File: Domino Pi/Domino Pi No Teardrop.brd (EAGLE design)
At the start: 71.1 x 33 mm, 73 parts, among them J1 MH28-1, J2 MH28-1, M1 DOMINO, SW1 IT-1100, U1 MP2162GQH, U2 CP2104-F03-GM, U3 74LVC1G125DCK

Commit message: Changed copyright
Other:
- board text added: "Reference designs are provided "AS IS" and "WITH ALL FAULTS". The Domino Team disclaims all other warranties express or implied, regarding this product, including but not limited to, any implied warranties of merchantibility or fitness for any particular application."
- board text added: "The Domino Team may make changes to specifications and product descriptions at any time, without notice."
- board text added: "© 2014, The Domino Team. All rights reserved."
- board text removed: "Michel Stempin may make changes to specifications and product descriptions at any time, without notice."
- board text removed: "Reference designs are provided "AS IS" and "WITH ALL FAULTS". Michel Stempin disclaims all other warranties express or implied, regarding this product, including but not limited to, any implied warranties of merchantibility or fitness for any particular application."
- board text removed: "© 2014, Michel Stempin. All rights reserved."
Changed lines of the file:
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@@
 See creativecommons.org/licenses/by-sa/4.0/</text>
 <text x="49.53" y="-50.8" size="0.8128" layer="48" ratio="20">Reference designs are provided "AS IS" and "WITH ALL FAULTS".
-Michel Stempin disclaims all other warranties express or implied,
+The Domino Team disclaims all other warranties express or implied,
 regarding this product, including but not limited to, any implied warranties of
 merchantibility or fitness for any particular application.</text>
-<text x="49.53" y="-54.61" size="0.8128" layer="48" ratio="20">Michel Stempin may make changes to specifications and product descriptions
+<text x="49.53" y="-54.61" size="0.8128" layer="48" ratio="20">The Domino Team may make changes to specifications and product descriptions
 at any time, without notice.</text>
-<text x="90.17" y="-40.64" size="1.27" layer="48" ratio="20">© 2014, Michel Stempin.
+<text x="90.17" y="-40.64" size="1.27" layer="48" ratio="20">© 2014, The Domino Team.
 All rights reserved.</text>
 <text x="95.25" y="-2.54" size="1.27" layer="48" ratio="10">NOTES:</text>

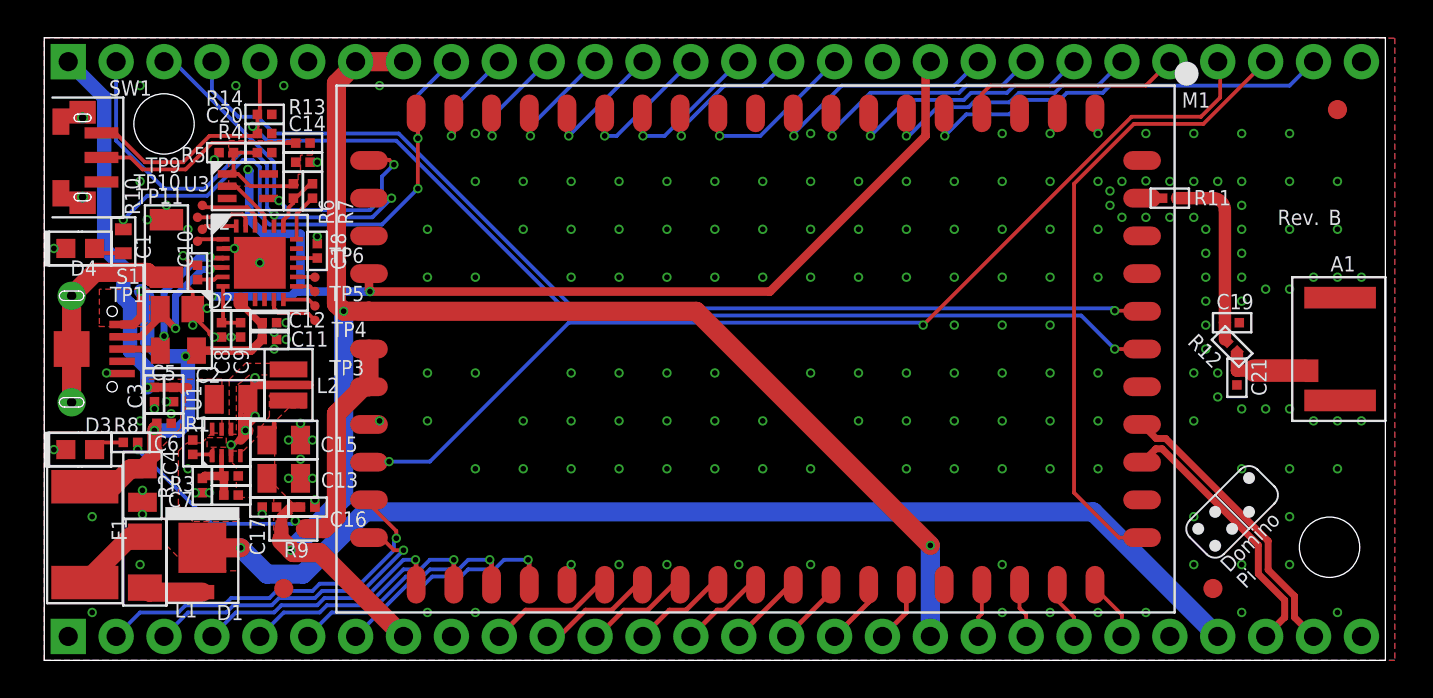
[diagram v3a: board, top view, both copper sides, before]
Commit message: Domino Pi rev. C: removed Schottky diode on +VUSB, it causes too much voltage drop, optimized power wiring, changed Logos
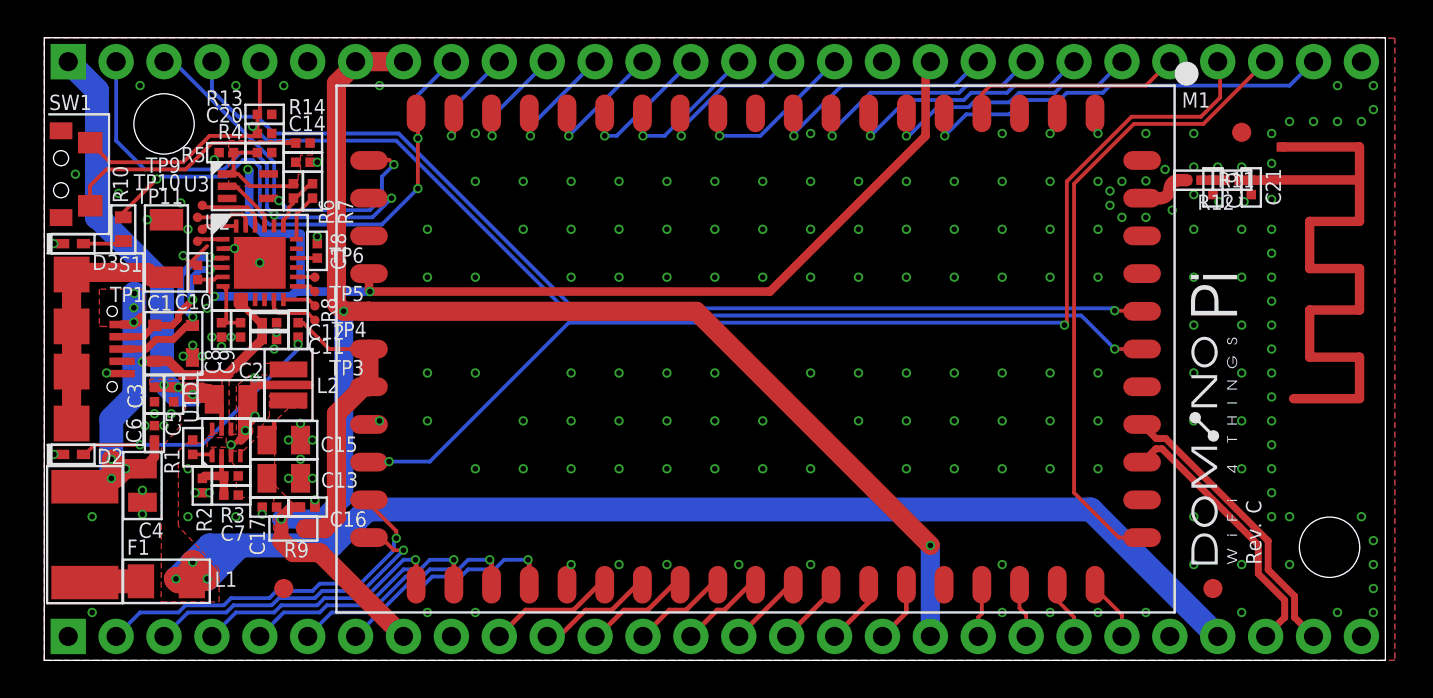
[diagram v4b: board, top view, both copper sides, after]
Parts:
- removed D4: BLUE, Domino:LED0603
- removed U$9: (no value), Domino:DOMINO_LOGO_SMALL
- added U$6, U$8: (no value), Domino:DOMINO_PI_LOGO_SMALL
- A1: value ACA-5036-A2-CC-S -> RF_ANT1; device Domino:ACA-5036-A2-CC-S -> Domino:RF_ANT1
- D1: value MBRM130LT1G -> PRTR5V0U2X; device Domino:DO-216AA -> Domino:SOT143B
- D2: value PRTR5V0U2X -> RED; device Domino:SOT143B -> Domino:LED0402
- D3: value RED -> BLUE; device Domino:LED0603 -> Domino:LED0402
- R13: value 1k -> 10k
- R14: value 10k -> 1k
- S1: value USB_MR5-003A -> USB_MR5-001; device Domino:USB_MR5-003A -> Domino:USB-MR5-001
- SW1: value IT-1100 -> IT-1210; device Domino:IT-1100 -> Domino:IT-1210
- U$7: value (none) -> DOMINO_PI_LOGO; device Domino:DOMINO_LOGO_SMALL -> Domino:DOMINO_PI_LOGO
- moved U$7 110.6 mm to (-33.0, -47.0)
- moved D1 12.6 mm to (6.86, 16.8), turned to 90 degrees
- moved A1 11.3 mm to (65.1, 27.2)
- moved D3 10.9 mm to (1.52, 22.1)
- moved R8 10.7 mm to (13.5, 17.5), turned to 90 degrees
- moved C21 10.1 mm to (64.0, 25.1)
- moved R12 8.83 mm to (63.0, 25.5), turned to 0 degrees
- moved D2 8.65 mm to (1.52, 10.9), turned to 0 degrees
- moved U$38 8.28 mm to (43.8, 19.7)
- moved C19 7.25 mm to (62.0, 25.1), turned to 270 degrees
- moved F4 5.22 mm to (63.5, 28.0)
- moved U$40 4.02 mm to (35.6, 14.0)
- moved U$41 3.81 mm to (10.2, 18.4)
- moved U$42 3.81 mm to (17.1, 18.4)
- moved R13 2.54 mm to (11.7, 29.0), turned to 180 degrees
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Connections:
- removed net +VUSB: D1.2, L1.1
- net +2V5: now also R14.2; no longer R13.2
- net +5V: now also L1.1; no longer D1.1
- net BLUE_LED: now also D3.2; no longer D4.2
- net D+: now also D1.2; no longer D2.3
- net D-: now also D1.3; no longer D2.2
- net GND: now also A1.GND, D1.1, R13.1, SW1.SH$1, SW1.SH$2; no longer A1.GND$1, A1.GND$2, D4.1, R14.1, SW1.S$1, SW1.S$2
- net JUMPSTART: now also R14.1, SW1.1; no longer R13.1, SW1.2
- net N$1: now also D2.2; no longer D3.2
- net PE: now also S1.SH$1, S1.SH$2, S1.SH$3, S1.SH$4; no longer S1.S$1, S1.S$2, S1.S$3
- net UART_RTS: now also R13.2, SW1.2; no longer R14.2, SW1.1
- net VBUS: now also D1.4; no longer D2.4
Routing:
- net +5V: track 79.5 -> 98.8 mm, vias 2 -> 6
- net N$1: track 1.68 -> 14.3 mm, vias 0 -> 2
- net ANT0_EXT: track 9.82 -> 1.27 mm
- net +3.3VD_IN: track 22.8 -> 16.2 mm, vias 2 -> 0
- net GPIO24: track 55.2 -> 59.6 mm
- net PE: track 11.3 -> 15.5 mm
- net ANT0_50R: track 4.98 -> 1.29 mm
- net +VUSB: track 3.21 -> 0.00 mm
- net VBUS: track 27.1 -> 30.1 mm, vias 3 -> 7
- net GND: track 19.0 -> 16.9 mm, vias 207 -> 213
- net JUMPSTART: track 11.1 -> 12.9 mm
- net ANT0: track 1.53 -> 3.19 mm
- net VPROT: track 4.19 -> 3.09 mm
- net D-: track 8.86 -> 7.82 mm
- net UART_TX: track 25.6 -> 24.8 mm
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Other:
- board text removed: "Domino Core"
- board text removed: "Domino Pi"
- board text removed: "Domino Qi"

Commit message: Domino Pi Rev. D: replaced resetable fuse by power swich, mino changes DC/DC layout and added more stitching vias
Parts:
- removed F4: FIDUCIAL, Domino:FIDUCIAL
- added C22: DNP, Domino:C0402
- added R15: 10k, Domino:R0402
- added R16: 0R, Domino:R0402
- added R17: 1k, Domino:R0402
- added U4: 74LVC1G125DCK, Domino:SC70
- C1: value 1n -> 10n; device Domino:C1206 -> Domino:C0402
- C11: value 1u -> 100n
- C12: value 100n -> 1u
- C13, C15: value 22u -> 100n; device Domino:C0805 -> Domino:C0402
- C14: value 100n -> 22u; device Domino:C0402 -> Domino:C0805
- C16, C3: value 10p -> 22u; device Domino:C0402 -> Domino:C0805
- C17: value 100n -> 10p
- C18: value 4u7 -> 100n
- C19: value DNP -> 4u7
- C2: value 22u -> 1n; device Domino:C0805 -> Domino:C1206
- C4: value 10u -> 10p; device Domino:C0805 -> Domino:C0402
- C7: value 22p -> 4u7; device Domino:C0402 -> Domino:C0805
- C8: value 4u7 -> 22p
- C9: value 100n -> 4u7
- F1: value 0ZCG0110FF2C -> FIDUCIAL; device Domino:PTC1812 -> Domino:FIDUCIAL
- R10: value 270R -> 0R; device Domino:R0603 -> Domino:R0402
- R11: value 0R -> 270R
- R12: device Domino:R0402 -> Domino:R0603
- R13: value 10k -> 270R; device Domino:R0402 -> Domino:R0603
- R14: value 1k -> 0R
- R3: value 150k -> 100k
- R4: value 47k -> 150k
- R5: value 47k -> 0R
- R6: value 0R -> 15k
- R7: value 0R -> 47k
- R8: value 270R -> 47k
- R9: device Domino:R0603 -> Domino:R0402
- U1: value MP2162GQH -> MP65151DJ; device Domino:QFN-8_2X1.5 -> Domino:SOT23-6
- U2: value CP2104-F03-GM -> MP2162GQH; device Domino:QFN-25_4X4 -> Domino:QFN-8_2X1.5
- U3: value 74LVC1G125DCK -> CP2104-F03-GM; device Domino:SC70 -> Domino:QFN-25_4X4
- moved R12 52.1 mm to (14.0, 7.75)
- moved F2 49.3 mm to (62.0, 3.81)
- moved R11 48.5 mm to (14.1, 13.0)
- moved C19 47.6 mm to (14.5, 21.7), turned to 90 degrees
- moved R14 47.3 mm to (61.0, 25.5)
- moved F3 24.2 mm to (63.5, 28.0)
- moved R5 24.1 mm to (1.27, 4.32), turned to 90 degrees
- moved R6 21.2 mm to (6.60, 4.70), turned to 270 degrees
- moved R9 17.9 mm to (13.2, 24.9), turned to 90 degrees
- moved R4 17.5 mm to (9.65, 9.53)
- moved C14 17.1 mm to (12.4, 9.40), turned to 0 degrees
- moved C15 14.8 mm to (13.7, 26.4), turned to 180 degrees
- moved C18 14.7 mm to (11.2, 7.37), turned to 270 degrees
- moved F1 10.9 mm to (12.7, 3.81), turned to 0 degrees
- moved R10 10.2 mm to (14.2, 24.9)
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- renumbered U$7 to W1
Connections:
- removed net VPROT: F1.1, L1.2
- new net !FLAG: R5.1, U1.4
- new net EN_USB: R3.1, R5.2, U1.3
- new net ILIM: R6.1, U1.5
- new net VIN: C5.1, C7.1, L1.1, R3.2, U1.1
- net !CTS: now also R10.1, U3.18; no longer R7.1, U2.18
- net !RTS: now also R10.2, R9.1, U3.19; no longer R6.1, R7.2, U2.19
- net !USB_UART: now also R7.2, R8.2, R9.2, U4.1; no longer R4.2, R5.2, R6.2, U3.1
- net +2V5: now also C11.1, C15.2, R17.2, R7.1, U4.5; no longer C10.1, C14.2, R14.2, R4.1, U2.5
- net +3.3VD_IN: now also R11.2, R12.2; no longer R8.2, R9.2
- net +3V3: now also C14.1, C18.1, C8.2, R12.1, R4.1, U2.4; no longer C13.1, C15.1, C7.2, R3.1, R9.1, U1.4
- net +5V: now also C4.1, C6.1, U1.6, U2.7; no longer C2.1, C5.1, L1.1, U1.7
- net ANT0: now also R14.1; no longer R11.1
- net ANT0_50R: now also C22.1, R16.2; no longer C21.1, R12.2
- net ANT0_EXT: now also C21.1, R14.2, R16.1; no longer C19.1, R11.2, R12.1
- net BLUE_LED: now also R13.1; no longer R10.1
- net D+: now also U3.3; no longer U2.3
- net D-: now also U3.4; no longer U2.4
- net EN: now also U2.1; no longer U1.1
- net FB: now also C8.1, R4.2, U2.2; no longer C7.1, R3.2, U1.2
- net GND: now also C14.2, C15.1, C22.2, C7.2, R15.1, R6.2, R8.1, U1.2, U2.3, U2.5, U3.2, U3.PAD, U4.3; no longer C14.1, C15.2, C8.2, R13.1, R5.1, U1.3, U1.5, U2.2, U2.PAD, U3.3
- net JUMPSTART: now also R17.1; no longer R14.1
- net LED0: now also R13.2; no longer R10.2
- net N$1: now also R11.1; no longer R8.1
- net N$12: now also U3.23; no longer U2.23
- net N$13: now also U3.24; no longer U2.24
- net N$15: now also U3.14; no longer U2.14
- net N$16: now also U3.13; no longer U2.13
- net N$2: now also U3.22; no longer U2.22
- net N$31: now also C19.1, U3.16; no longer C18.1, U2.16
- net N$6: now also U3.1; no longer U2.1
- net N$8: now also U3.11; no longer U2.11
- net N$9: now also U3.12; no longer U2.12
- net PE: now also C2.1; no longer C1.1
- net SW: now also U2.6; no longer U1.6
- net TXD: now also U3.21, U4.2; no longer U2.21, U3.2
- net UART_RTS: now also R15.2; no longer R13.2
- net UART_RX: now also U4.4; no longer U3.4
- net UART_TX: now also U3.20; no longer U2.20
- net VBUS: now also C1.1, C13.1, L1.2, U3.7, U3.8; no longer C11.1, C4.1, C6.1, F1.2, U2.7, U2.8
- net VDD: now also C10.1, U3.6; no longer C8.1, U2.6
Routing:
- net +5V: track 98.8 -> 86.7 mm, vias 6 -> 5
- net VBUS: track 30.1 -> 20.3 mm, vias 7 -> 6
- net GND: track 16.9 -> 9.52 mm, vias 213 -> 237
- net +3.3VD_IN: track 16.2 -> 10.8 mm
- net +3V3: track 84.3 -> 79.8 mm, vias 3 -> 4
- net !FLAG: track 0.00 -> 4.36 mm
- net VPROT: track 3.09 -> 0.00 mm
- net EN_USB: track 0.00 -> 2.87 mm
- net UART_RTS: track 66.2 -> 69.0 mm
- net UART_CTS: track 55.7 -> 58.5 mm
- net GPIO24: track 59.6 -> 61.5 mm
- net ILIM: track 0.00 -> 1.37 mm
- net N$1: track 14.3 -> 13.0 mm
- added copper zone on layer 1, net VIN
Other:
- board text added: "© 2014-2015, The Domino Team. All rights reserved."
- board text removed: "SLOT SIZE IN MM 2x PLATED SLOT: 0.9x0.4"
- board text removed: "SLOT SIZE IN MM 2x PLATED SLOT: 1.3x0.5"
- board text removed: "© 2014, The Domino Team. All rights reserved."

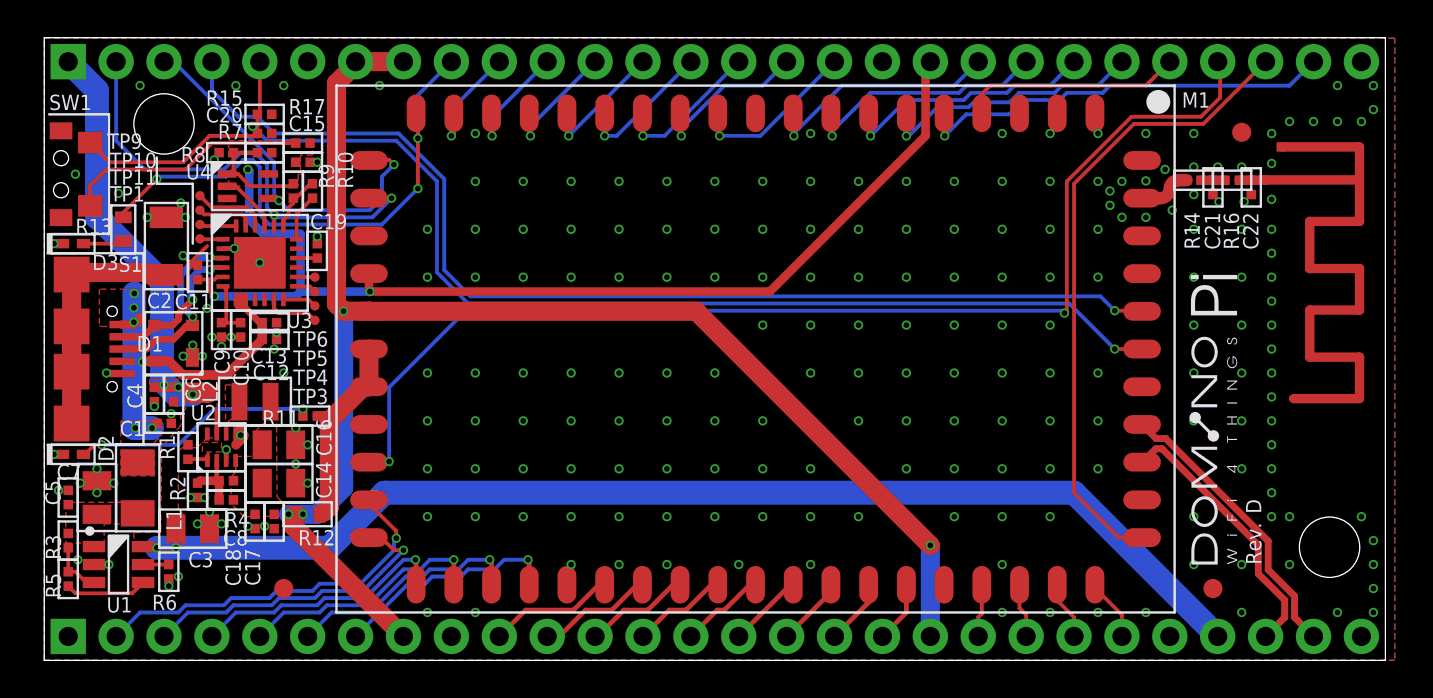
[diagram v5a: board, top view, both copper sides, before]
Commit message: Domino Pi Rev. D: added some vias, spaced antenna pi network components and removed solder paste from antenna
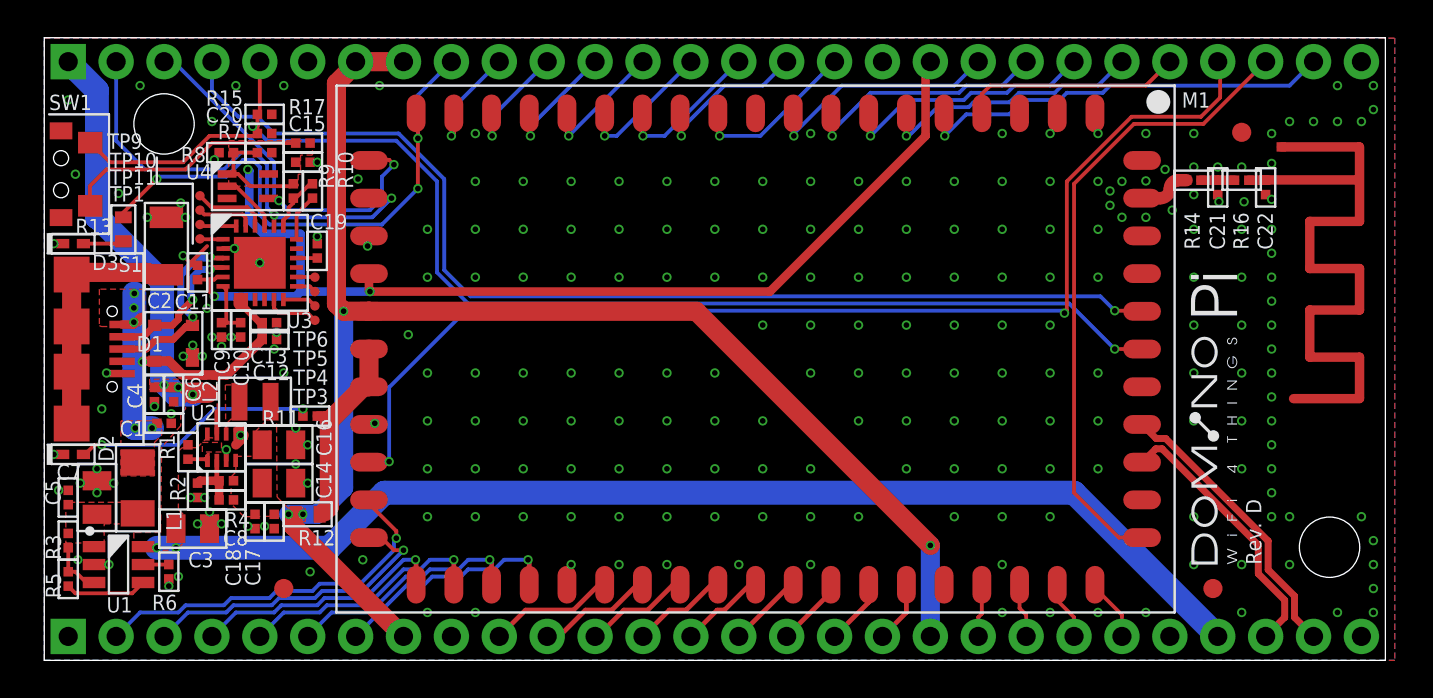
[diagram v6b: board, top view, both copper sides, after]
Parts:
- moved C22 0.76 mm to (64.8, 25.1)
- moved R16 0.51 mm to (63.5, 25.5)
- moved C21 0.25 mm to (62.2, 25.1)
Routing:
- net ANT0_EXT: track 1.27 -> 1.78 mm
- net GND: vias 237 -> 246
